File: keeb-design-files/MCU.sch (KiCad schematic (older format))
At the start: 34 parts, among them J1 Conn_ARM_JTAG_SWD_10, J2 SMA, J6 Conn_01x04, SW1 RESET, SW70 BOOT0, U1 STM32L452CEUx, U2 nRF24L01P, Y2 Crystal_GND24

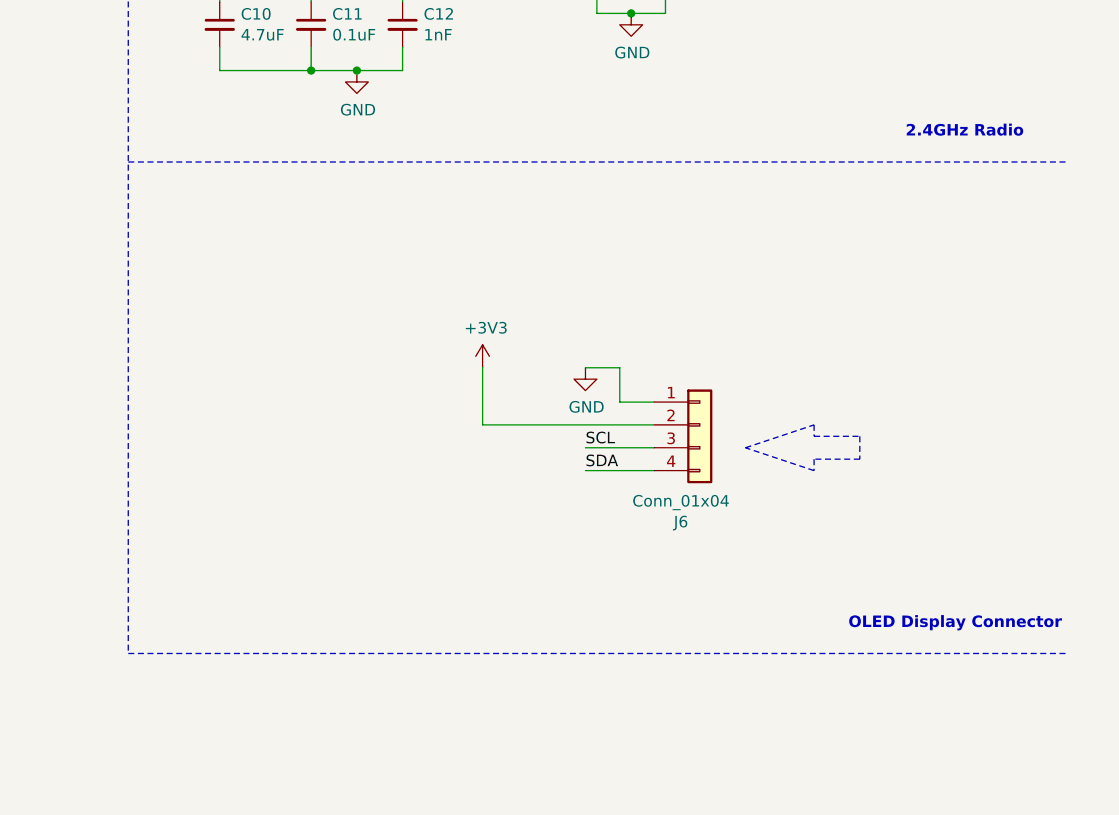
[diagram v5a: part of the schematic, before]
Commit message: Add I2C Pull-ups, Add STC3100 Fuel Guage
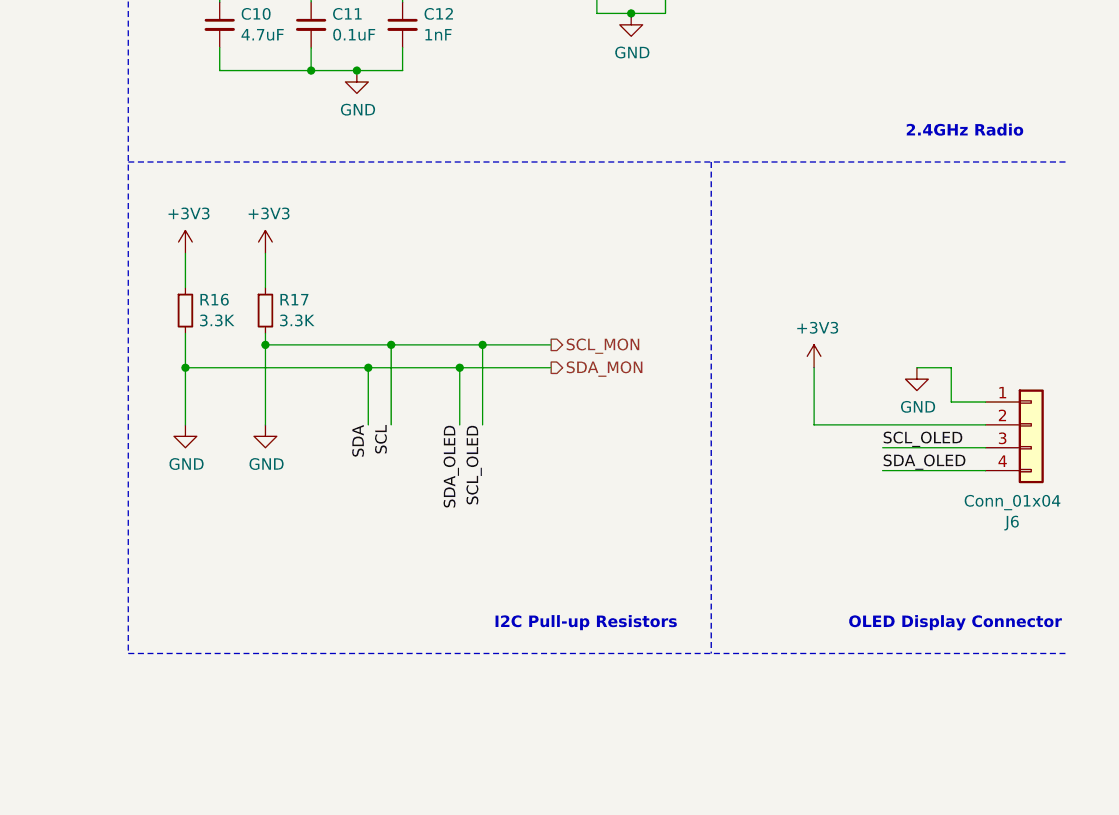
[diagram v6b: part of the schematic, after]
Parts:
- added R16, R17: 3.3K, Resistor_SMD:R_0603_1608Metric_Pad1.05x0.95mm_HandSolder, symbol Device:R_Small
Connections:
- net SCL is gone; now on net GND: J6.3 (Pin_3), U1.30 (PA9)
- net SDA is gone; now on net GND: J6.4 (Pin_4), U1.31 (PA10)
- net +3V3: now also R16.1, R17.1
- net GND: now also R16.2, R17.2
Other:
- note added: "I2C Pull-up Resistors"
- moved on the sheet: J6
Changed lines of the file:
@@
 L Connector_Generic:Conn_01x04 J6
 U 1 1 5EC1B74C
-P 9450 5450
-F 0 "J6" H 9368 5025 50  0000 C CNN
-F 1 "Conn_01x04" H 9368 5116 50  0000 C CNN
-F 2 "lib_fp:OLED_Display" H 9450 5450 50  0001 C CNN
-F 3 "~" H 9450 5450 50  0001 C CNN
-	1    9450 5450
+P 10900 5450
+F 0 "J6" H 10818 5025 50  0000 C CNN
+F 1 "Conn_01x04" H 10818 5116 50  0000 C CNN
+F 2 "lib_fp:OLED_Display" H 10900 5450 50  0001 C CNN
+F 3 "~" H 10900 5450 50  0001 C CNN
+	1    10900 5450
 	1    0    0    -1
 $EndComp
@@
 L power:GND #PWR0147
 U 1 1 5EC1C40E
-P 8950 5200
-F 0 "#PWR0147" H 8950 4950 50  0001 C CNN
-F 1 "GND" H 8955 5027 50  0000 C CNN
-F 2 "" H 8950 5200 50  0001 C CNN
-F 3 "" H 8950 5200 50  0001 C CNN
-	1    8950 5200
+P 10400 5200
+F 0 "#PWR0147" H 10400 4950 50  0001 C CNN
+F 1 "GND" H 10405 5027 50  0000 C CNN
+F 2 "" H 10400 5200 50  0001 C CNN
+F 3 "" H 10400 5200 50  0001 C CNN
+	1    10400 5200
 	1    0    0    -1
 $EndComp
 Wire Wire Line
-	8950 5200 9100 5200
+	10400 5200 10550 5200
 $Comp
 L power:+3V3 #PWR0148
 U 1 1 5EC263E6
-P 8500 5200
-F 0 "#PWR0148" H 8500 5050 50  0001 C CNN
-F 1 "+3V3" H 8515 5373 50  0000 C CNN
-F 2 "" H 8500 5200 50  0001 C CNN
-F 3 "" H 8500 5200 50  0001 C CNN
-	1    8500 5200
+P 9950 5200
+F 0 "#PWR0148" H 9950 5050 50  0001 C CNN
+F 1 "+3V3" H 9965 5373 50  0000 C CNN
+F 2 "" H 9950 5200 50  0001 C CNN
+F 3 "" H 9950 5200 50  0001 C CNN
+	1    9950 5200
 	1    0    0    -1
 $EndComp
 Wire Wire Line
-	8500 5200 8500 5450
+	9950 5200 9950 5450
 Wire Wire Line
-	8500 5450 9250 5450
-Text Label 8950 5550 0    50   ~ 0
-SCL
+	9950 5450 10700 5450
+Text Label 10250 5550 0    50   ~ 0
+SCL_OLED
 Wire Wire Line
-	8950 5550 9250 5550
-Text Label 8950 5650 0    50   ~ 0
-SDA
+	10250 5550 10700 5550
+Text Label 10250 5650 0    50   ~ 0
+SDA_OLED
 Wire Wire Line
-	8950 5650 9250 5650
+	10250 5650 10700 5650
 Wire Wire Line
-	9100 5200 9100 5350
+	10550 5200 10550 5350
 Wire Wire Line
-	9100 5350 9250 5350
+	10550 5350 10700 5350
 Text Label 5500 3550 2    50   ~ 0
 SCL
@@
 Wire Wire Line
 	3650 3950 3850 3950
-Wire Notes Line
-	9650 5550 9950 5450
-Wire Notes Line
-	9950 5650 9650 5550
-Wire Notes Line
-	9950 5450 9950 5500
-Wire Notes Line
-	9950 5500 10150 5500
-Wire Notes Line
-	10150 5500 10150 5600
-Wire Notes Line
-	10150 5600 9950 5600
-Wire Notes Line
-	9950 5600 9950 5650
 Text Notes 10100 6350 0    50   ~ 10
 OLED Display Connector
@@
 Text Notes 700  5600 0    50   ~ 10
 SWD/JTAG Connector
+$Comp
+L Device:R_Small R16
+U 1 1 5ED439B8
+P 7200 4950
+F 0 "R16" H 7259 4996 50  0000 L CNN
+F 1 "3.3K" H 7259 4905 50  0000 L CNN
+F 2 "Resistor_SMD:R_0603_1608Metric_Pad1.05x0.95mm_HandSolder" H 7200 4950 50  0001 C CNN
+F 3 "~" H 7200 4950 50  0001 C CNN
+F 4 "C22978" H 7259 4859 50  0001 L CNN "LCSC Part Number"
+	1    7200 4950
+	1    0    0    -1
+$EndComp
+$Comp
+L Device:R_Small R17
+U 1 1 5ED44595
+P 7550 4950
+F 0 "R17" H 7609 4996 50  0000 L CNN
+F 1 "3.3K" H 7609 4905 50  0000 L CNN
+F 2 "Resistor_SMD:R_0603_1608Metric_Pad1.05x0.95mm_HandSolder" H 7550 4950 50  0001 C CNN
+F 3 "~" H 7550 4950 50  0001 C CNN
+F 4 "C22978" H 7609 4859 50  0001 L CNN "LCSC Part Number"
+	1    7550 4950
+	1    0    0    -1
+$EndComp
+$Comp
+L power:+3V3 #PWR0153
+U 1 1 5ED452C7
+P 7200 4700
+F 0 "#PWR0153" H 7200 4550 50  0001 C CNN
+F 1 "+3V3" H 7215 4873 50  0000 C CNN
+F 2 "" H 7200 4700 50  0001 C CNN
+F 3 "" H 7200 4700 50  0001 C CNN
+	1    7200 4700
+	1    0    0    -1
+$EndComp
+$Comp
+L power:+3V3 #PWR0154
+U 1 1 5ED45C03
+P 7550 4700
+F 0 "#PWR0154" H 7550 4550 50  0001 C CNN
+F 1 "+3V3" H 7565 4873 50  0000 C CNN
+F 2 "" H 7550 4700 50  0001 C CNN
+F 3 "" H 7550 4700 50  0001 C CNN
+	1    7550 4700
+	1    0    0    -1
+$EndComp
+$Comp
+L power:GND #PWR0155
+U 1 1 5ED46250
+P 7200 5450
+F 0 "#PWR0155" H 7200 5200 50  0001 C CNN
+F 1 "GND" H 7205 5277 50  0000 C CNN
+F 2 "" H 7200 5450 50  0001 C CNN
+F 3 "" H 7200 5450 50  0001 C CNN
+	1    7200 5450
+	1    0    0    -1
+$EndComp
+$Comp
+L power:GND #PWR0156
+U 1 1 5ED46B47
+P 7550 5450
+F 0 "#PWR0156" H 7550 5200 50  0001 C CNN
+F 1 "GND" H 7555 5277 50  0000 C CNN
+F 2 "" H 7550 5450 50  0001 C CNN
+F 3 "" H 7550 5450 50  0001 C CNN
+	1    7550 5450
+	1    0    0    -1
+$EndComp
+Wire Wire Line
+	7200 4850 7200 4700
+Wire Wire Line
+	7550 4700 7550 4850
+Wire Wire Line
+	7200 5450 7200 5200
+Wire Wire Line
+	7550 5050 7550 5100
+Text HLabel 8800 5100 2    50   Output ~ 0
+SCL_MON
+Text HLabel 8800 5200 2    50   Output ~ 0
+SDA_MON
+Wire Wire Line
+	8800 5100 8500 5100
+Connection ~ 7550 5100
+Wire Wire Line
+	7550 5100 7550 5450
+Connection ~ 7200 5200
+Wire Wire Line
+	7200 5200 7200 5050
+Text Label 8000 5450 3    50   ~ 0
+SDA
+Text Label 8100 5450 3    50   ~ 0
+SCL
+Wire Wire Line
+	8000 5450 8000 5200
+Connection ~ 8000 5200
+Wire Wire Line
+	8000 5200 7200 5200
+Wire Wire Line
+	8000 5200 8400 5200
+Wire Wire Line
+	8100 5450 8100 5100
+Connection ~ 8100 5100
+Wire Wire Line
+	8100 5100 7550 5100
+Text Label 8400 5450 3    50   ~ 0
+SDA_OLED
+Wire Wire Line
+	8400 5450 8400 5200
+Connection ~ 8400 5200
+Wire Wire Line
+	8400 5200 8800 5200
+Text Label 8500 5450 3    50   ~ 0
+SCL_OLED
+Wire Wire Line
+	8500 5450 8500 5100
+Connection ~ 8500 5100
+Wire Wire Line
+	8500 5100 8100 5100
+Wire Notes Line width 20
+	9500 4300 9500 6450
+Text Notes 8550 6350 0    50   ~ 10
+I2C Pull-up Resistors
 $EndSCHEMATC

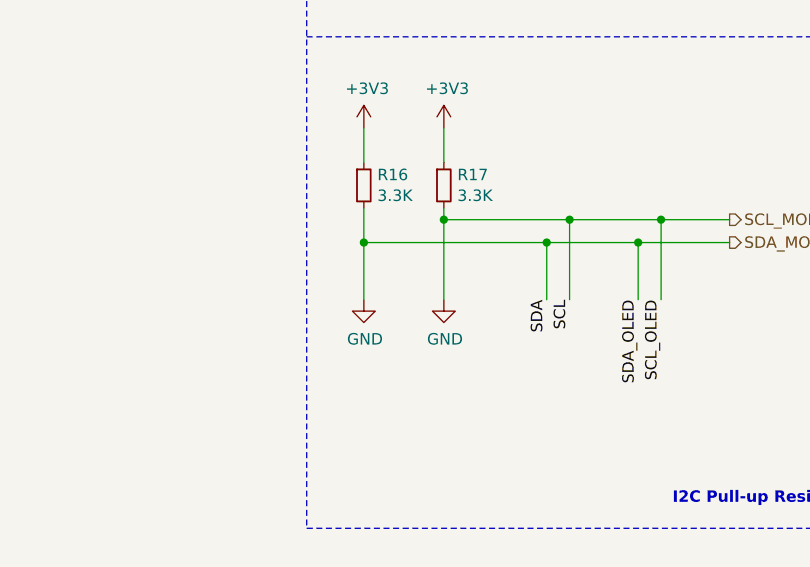
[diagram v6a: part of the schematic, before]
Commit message: Confirm LCSC part numbers, started placement for layout
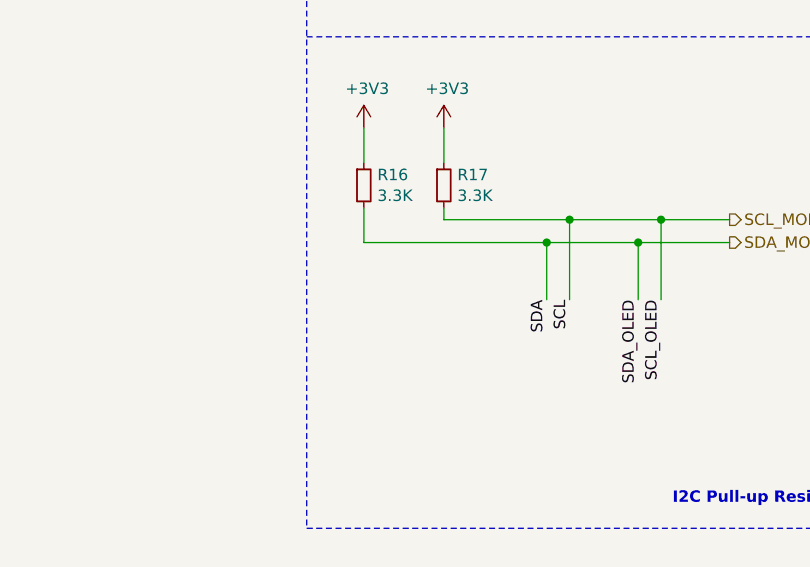
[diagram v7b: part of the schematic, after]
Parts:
- R3: footprint (none) -> Resistor_SMD:R_0603_1608Metric_Pad1.05x0.95mm_HandSolder
- R7: footprint (none) -> Resistor_SMD:R_0402_1005Metric
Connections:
- net GND: no longer J6.3 (Pin_3), J6.4 (Pin_4), R16.2, R17.2, U1.30 (PA9), U1.31 (PA10)
- new net SCL_MON: J6.3 (Pin_3), R17.2, U1.30 (PA9)
- new net SDA_MON: J6.4 (Pin_4), R16.2, U1.31 (PA10)
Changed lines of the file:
@@
 F 0 "R3" V 9250 3300 50  0000 C CNN
 F 1 "1M" V 9300 3300 50  0000 C CNN
-F 2 "" H 9150 3300 50  0001 C CNN
+F 2 "Resistor_SMD:R_0603_1608Metric_Pad1.05x0.95mm_HandSolder" H 9150 3300 50  0001 C CNN
 F 3 "~" H 9150 3300 50  0001 C CNN
 	1    9150 3300
@@
 F 0 "R7" H 2759 1596 50  0000 L CNN
 F 1 "22K" H 2759 1505 50  0000 L CNN
-F 2 "" H 2700 1550 50  0001 C CNN
+F 2 "Resistor_SMD:R_0402_1005Metric" H 2700 1550 50  0001 C CNN
 F 3 "~" H 2700 1550 50  0001 C CNN
 F 4 "C25768" H 2700 1550 50  0001 C CNN "LCSC Part Number"
@@
 	1    0    0    -1
 $EndComp
-$Comp
-L power:GND #PWR0155
-U 1 1 5ED46250
-P 7200 5450
-F 0 "#PWR0155" H 7200 5200 50  0001 C CNN
-F 1 "GND" H 7205 5277 50  0000 C CNN
-F 2 "" H 7200 5450 50  0001 C CNN
-F 3 "" H 7200 5450 50  0001 C CNN
-	1    7200 5450
-	1    0    0    -1
-$EndComp
-$Comp
-L power:GND #PWR0156
-U 1 1 5ED46B47
-P 7550 5450
-F 0 "#PWR0156" H 7550 5200 50  0001 C CNN
-F 1 "GND" H 7555 5277 50  0000 C CNN
-F 2 "" H 7550 5450 50  0001 C CNN
-F 3 "" H 7550 5450 50  0001 C CNN
-	1    7550 5450
-	1    0    0    -1
-$EndComp
 Wire Wire Line
 	7200 4850 7200 4700
 Wire Wire Line
 	7550 4700 7550 4850
-Wire Wire Line
-	7200 5450 7200 5200
 Wire Wire Line
 	7550 5050 7550 5100
@@
 Wire Wire Line
 	8800 5100 8500 5100
-Connection ~ 7550 5100
-Wire Wire Line
-	7550 5100 7550 5450
-Connection ~ 7200 5200
 Wire Wire Line
 	7200 5200 7200 5050
